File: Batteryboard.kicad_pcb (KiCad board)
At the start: 4 copper layers, 76.2 x 76.2 mm, 156 parts, among them IC1 FAN4010IL6X_F113, IC2 FAN4010IL6X_F113, IC3 FAN4010IL6X_F113, J1 Conn_01x02_Male, J2 Conn_01x03_Male, J3 Conn_01x05_Male, J4 Conn_01x02_Male, J5 SC_19-20, Q1 SI7617DN-T1-GE3, Q2 SI7617DN-T1-GE3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

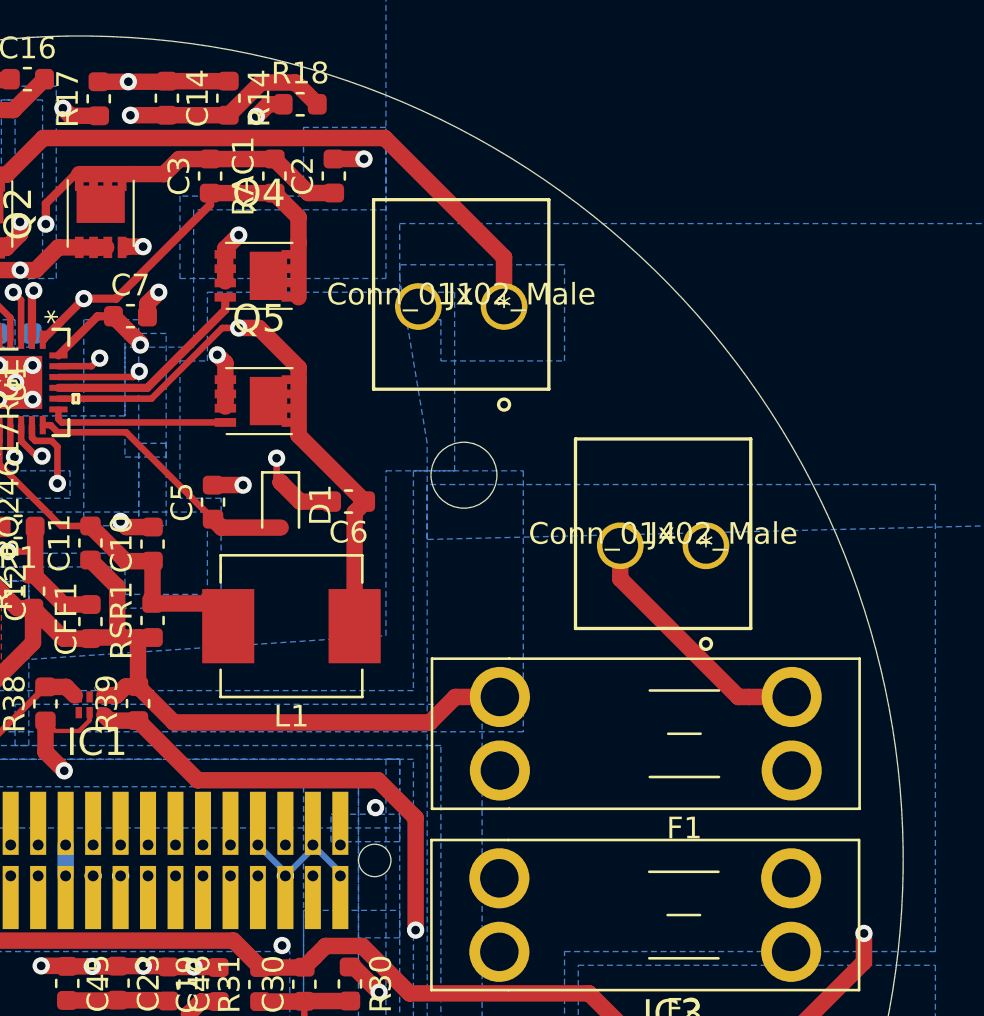
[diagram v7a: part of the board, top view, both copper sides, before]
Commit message: added 4 pin for AOA sensor
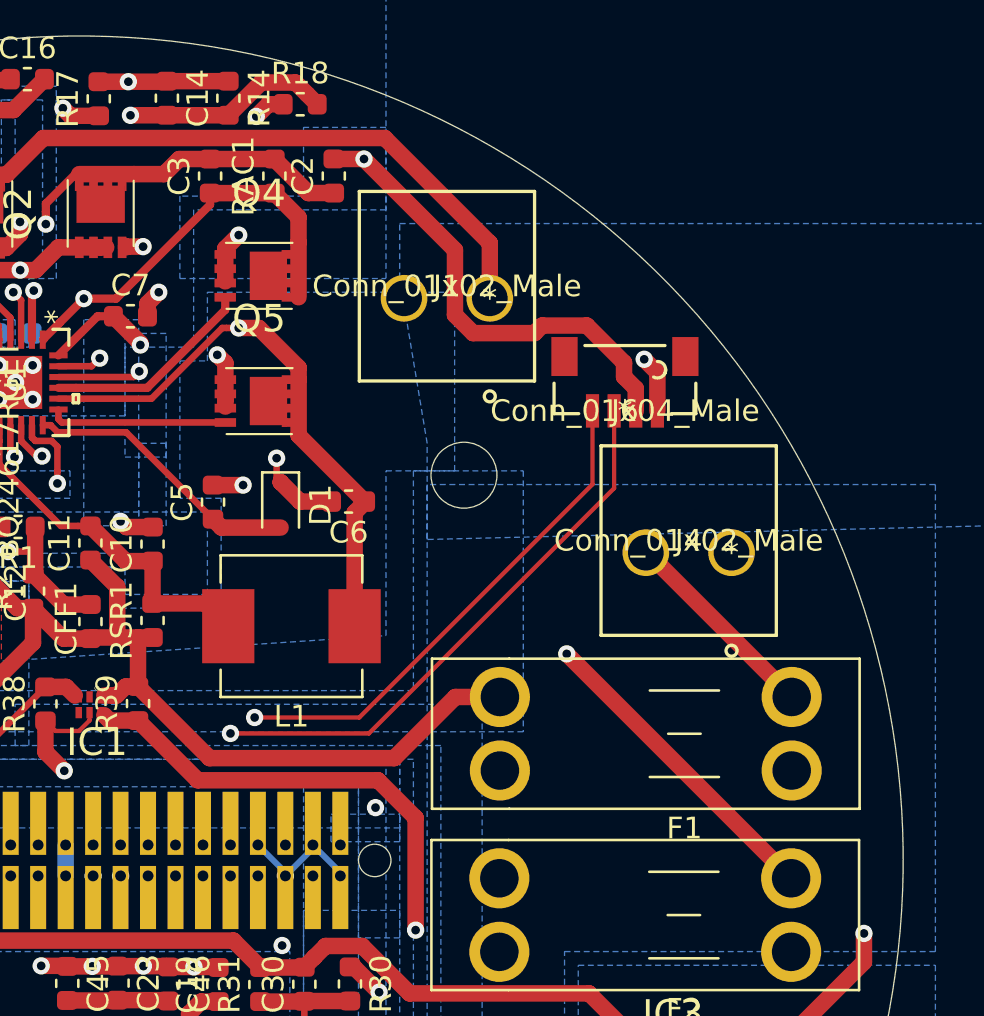
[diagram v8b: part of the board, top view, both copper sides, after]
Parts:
- added J6: Conn_01x04_Male, 5013310407:1734595-4, F.Cu at (260.6, 42.3)
- moved J4 1.22 mm to (265.5, 48.9)
- moved J1 0.76 mm to (254.4, 37.1)
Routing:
- net CAN_H: track 27.3 -> 65.7 mm, vias 2 -> 3
- net CAN_L: track 31.5 -> 67.9 mm, vias 2 -> 3
- net VSS: track 120.3 -> 140.8 mm
- net 5V0: track 34.9 -> 37.5 mm, vias 13 -> 14
- net Net-(F1-Pad1): track 15.1 -> 12.9 mm
- net Q6S: track 88.2 -> 90.4 mm
- net SRN: track 67.0 -> 68.4 mm
- net Net-(J1-Pad1): track 42.7 -> 42.0 mm
- net Net-(F2-Pad1): vias 1 -> 2
